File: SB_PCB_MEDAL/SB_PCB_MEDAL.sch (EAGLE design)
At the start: 41 parts, among them IC1 ATTINY44A-SSU

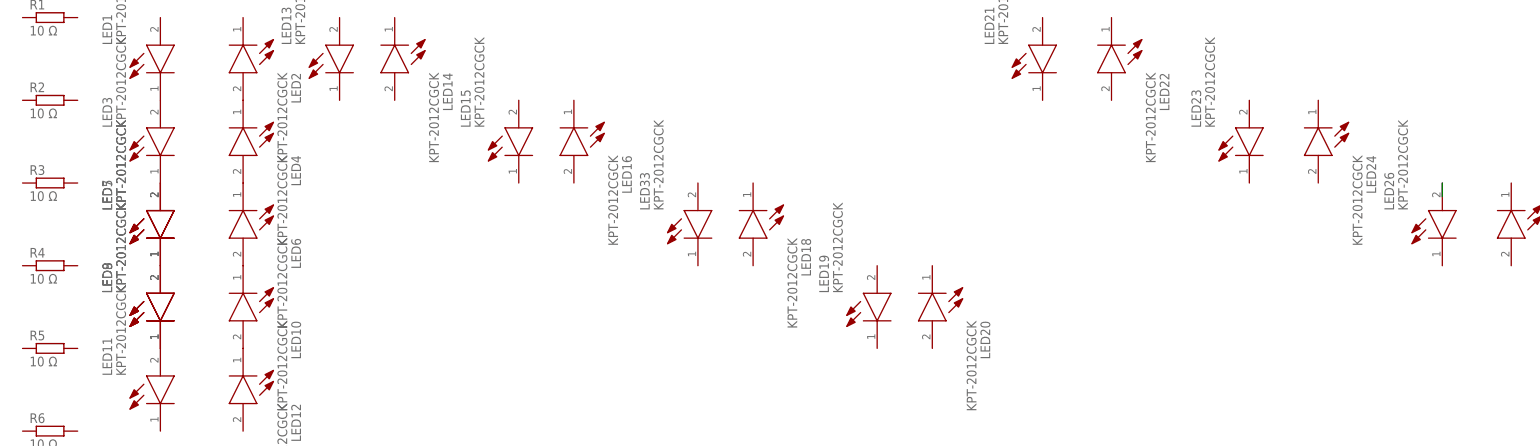
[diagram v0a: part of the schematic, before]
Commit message: removed 2 additional LEDs
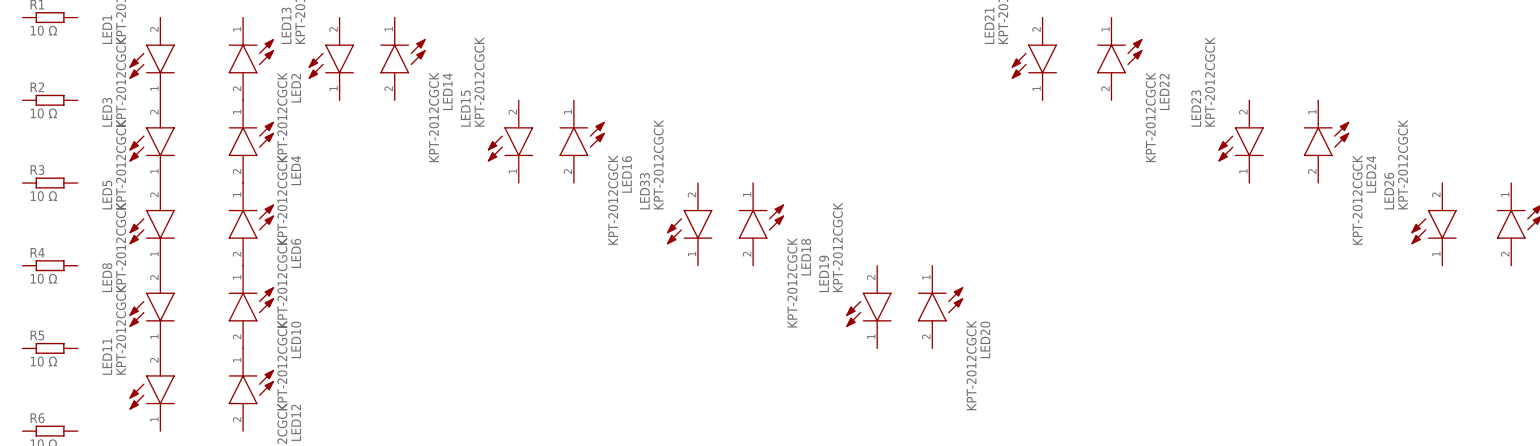
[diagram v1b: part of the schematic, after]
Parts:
- removed LED7, LED9: KPT-2012CGCK, SamacSys_Parts:KPT-2012CGCK
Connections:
- removed net N$1: LED26.A
- net N$2: no longer LED7.A
- net N$4: no longer LED7.K, LED9.A
- net N$5: no longer LED9.K
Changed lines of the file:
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@@
 <?xml version="1.0" encoding="utf-8"?>
 <!DOCTYPE eagle SYSTEM "eagle.dtd">
-<eagle version="7.6.0">
+<eagle version="8.4.1">
 <drawing>
 <settings>
 <setting alwaysvectorfont="no"/>
+<setting keepoldvectorfont="yes"/>
 <setting verticaltext="up"/>
 </settings>
@@
 <part name="LED5" library="SamacSys_Parts" deviceset="KPT-2012CGCK" device=""/>
 <part name="LED6" library="SamacSys_Parts" deviceset="KPT-2012CGCK" device=""/>
-<part name="LED7" library="SamacSys_Parts" deviceset="KPT-2012CGCK" device=""/>
 <part name="LED8" library="SamacSys_Parts" deviceset="KPT-2012CGCK" device=""/>
-<part name="LED9" library="SamacSys_Parts" deviceset="KPT-2012CGCK" device=""/>
 <part name="LED10" library="SamacSys_Parts" deviceset="KPT-2012CGCK" device=""/>
 <part name="LED11" library="SamacSys_Parts" deviceset="KPT-2012CGCK" device=""/>
@@
 <instance part="LED5" gate="G$1" x="144.78" y="25.4" rot="R90"/>
 <instance part="LED6" gate="G$1" x="160.02" y="40.64" rot="R270"/>
-<instance part="LED7" gate="G$1" x="144.78" y="25.4" rot="R90"/>
 <instance part="LED8" gate="G$1" x="144.78" y="10.16" rot="R90"/>
-<instance part="LED9" gate="G$1" x="144.78" y="10.16" rot="R90"/>
 <instance part="LED10" gate="G$1" x="160.02" y="25.4" rot="R270"/>
 <instance part="LED11" gate="G$1" x="144.78" y="-5.08" rot="R90"/>
@@
 </segment>
 </net>
-<net name="N$1" class="0">
-<segment>
-<pinref part="LED26" gate="G$1" pin="A"/>
-<wire x1="381" y1="40.64" x2="381" y2="38.1" width="0.1524" layer="91"/>
-</segment>
-</net>
 <net name="N$3" class="0">
 <segment>
@@
 <pinref part="LED3" gate="G$1" pin="K"/>
 <pinref part="LED5" gate="G$1" pin="A"/>
-<pinref part="LED7" gate="G$1" pin="A"/>
 </segment>
 </net>
@@
 <segment>
 <pinref part="LED5" gate="G$1" pin="K"/>
-<pinref part="LED7" gate="G$1" pin="K"/>
 <pinref part="LED8" gate="G$1" pin="A"/>
-<pinref part="LED9" gate="G$1" pin="A"/>
 </segment>
 </net>
@@
 <segment>
 <pinref part="LED8" gate="G$1" pin="K"/>
-<pinref part="LED9" gate="G$1" pin="K"/>
 <pinref part="LED11" gate="G$1" pin="A"/>
 </segment>

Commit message: literally copy and paste files from other branch into the master because EAGLE files and branches hate each other as much as North Korea and the US....
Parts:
- removed LED31, LED32, LED33: KPT-2012CGCK, SamacSys_Parts:KPT-2012CGCK
- added LED17, LED7, LED9: KPT-2012CGCK, SamacSys_Parts:KPT-2012CGCK
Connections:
- removed net N$10: LED2.A, LED4.K
- removed net N$7: LED10.K, LED6.A
- removed net N$8: LED4.A, LED6.K
- new net N$1: LED1.A, LED11.A, LED12.K, LED19.A, LED2.K, LED20.K, LED25.A, LED26.K, LED29.A, LED30.K, R1.2
- new net N$19: IC1.[PCINT10/INT0/OC0A/CKOUT]PB2
- new net N$20: IC1.[PCINT7/ICP/OC0B/ADC7]PA7
- new net PA0: IC1.PA0[ADC0/AREF/PCINT0], R1.1
- new net PA1: IC1.PA1[ADC1/AIN0/PCINT1], R2.1
- new net PA2: IC1.PA2[ADC2/AIN1/PCINT2], R3.1
- new net PA3: IC1.PA3[ADC3/T0/PCINT3], R4.1
- new net PB0: IC1.[PCINT8/XTAL1/CLKI]PB0, R5.1
- new net PB1: IC1.[PCINT9/XTAL2]PB1, R6.1
- net N$2: now also LED1.K, LED13.A, LED14.K, LED2.A, LED21.A, LED22.K, LED27.A, LED28.K, LED3.A, LED4.K, R2.2; no longer LED3.K, LED5.A
- net N$3: now also LED11.K, LED12.A, LED15.A, LED16.K, LED23.A, LED24.K, LED3.K, LED4.A, LED5.A, LED6.K, R3.2; no longer LED1.K, LED3.A
- net N$4: now also LED13.K, LED14.A, LED17.A, LED18.K, LED19.K, LED20.A, LED6.A, LED7.A, LED8.K, R4.2; no longer LED8.A
- net N$5: now also LED10.K, LED15.K, LED16.A, LED21.K, LED22.A, LED25.K, LED26.A, LED7.K, LED8.A, LED9.A, R5.2; no longer LED11.A, LED8.K
- net N$6: now also LED17.K, LED18.A, LED23.K, LED24.A, LED27.K, LED28.A, LED29.K, LED30.A, LED9.K, R6.2; no longer LED12.K
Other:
- note added: "PA0"
- note added: "PA1"
- note added: "PA2"
- note added: "PA3"
- note added: "PB0"
- note added: "PB1"
- moved on the sheet: LED1, LED10, LED11, LED12, LED13, LED14, LED15, LED16, LED18, LED19, LED2, LED20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

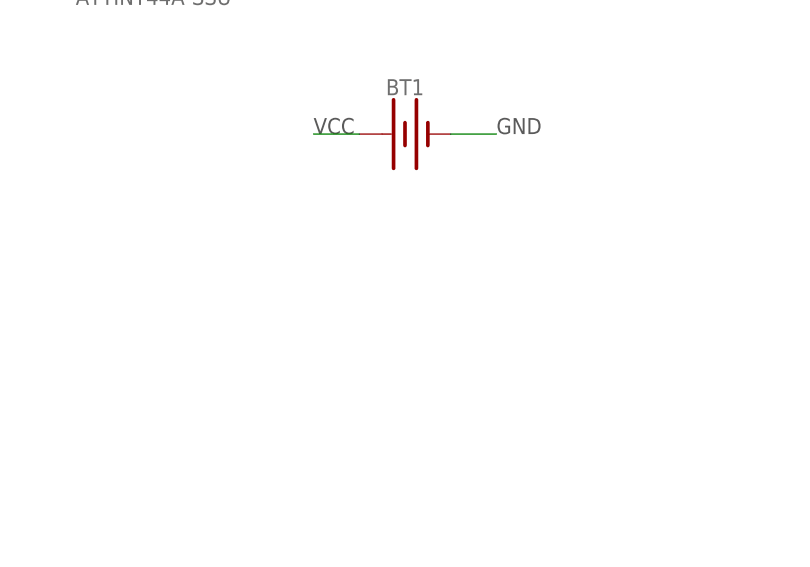
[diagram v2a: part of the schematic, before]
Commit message: added surface mountable button
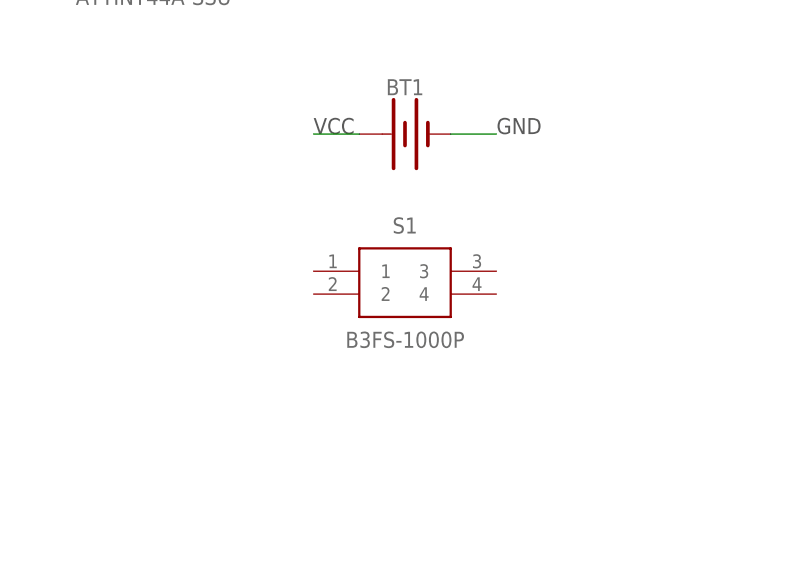
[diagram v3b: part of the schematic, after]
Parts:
- added S1: B3FS-1000P, SamacSys_Parts:B3FS-1000P
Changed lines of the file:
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@@
 <part name="LED29" library="SamacSys_Parts" deviceset="KPT-2012CGCK" device=""/>
 <part name="LED30" library="SamacSys_Parts" deviceset="KPT-2012CGCK" device=""/>
+<part name="S1" library="SamacSys_Parts" deviceset="B3FS-1000P" device=""/>
 </parts>
 <sheets>
@@
 <instance part="LED29" gate="G$1" x="431.8" y="66.04" rot="R90"/>
 <instance part="LED30" gate="G$1" x="441.96" y="81.28" rot="R270"/>
+<instance part="S1" gate="G$1" x="58.42" y="15.24"/>
 </instances>
 <busses>

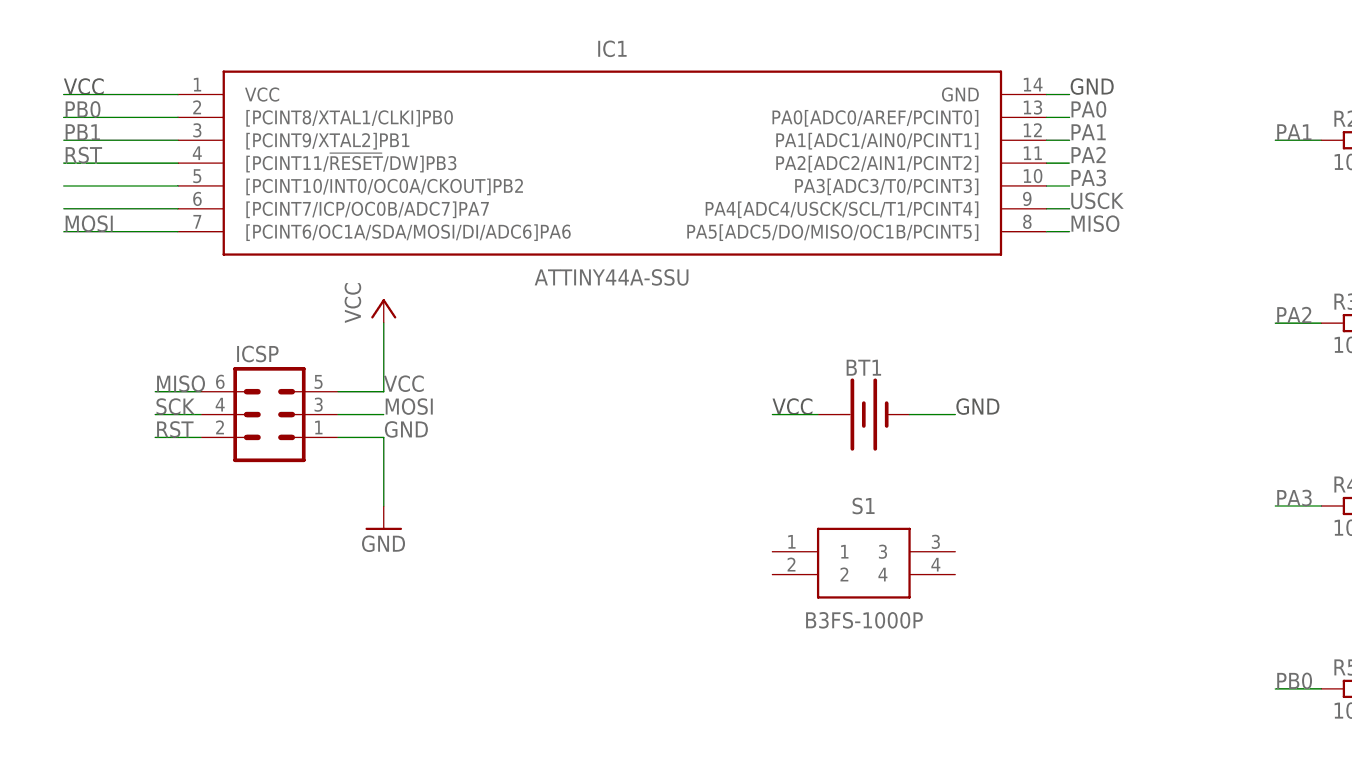
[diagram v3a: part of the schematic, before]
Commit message: added more labels to the board
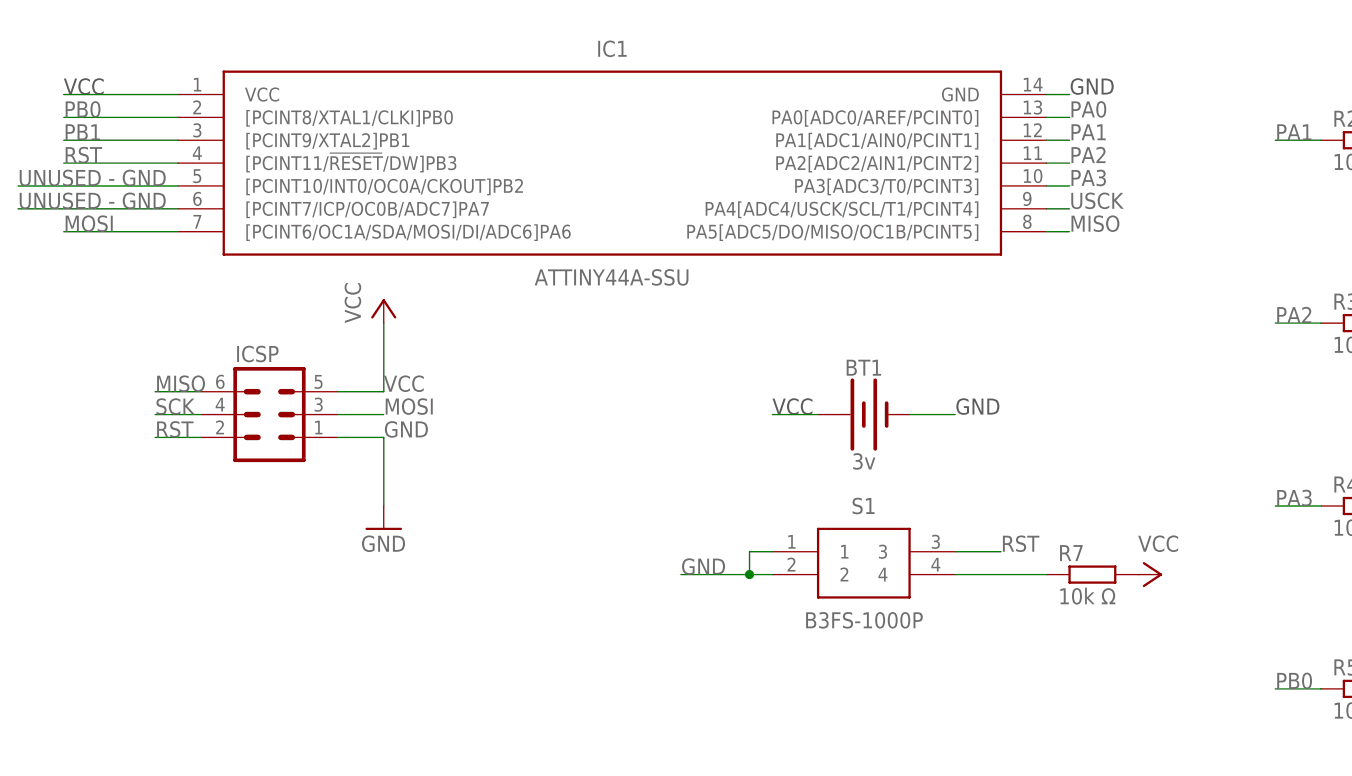
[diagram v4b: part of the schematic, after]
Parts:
- added R7: 10k Ω, resistor:R-EU_M0805
- BT1: value (none) -> 3v
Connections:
- removed net N$19: IC1.[PCINT10/INT0/OC0A/CKOUT]PB2
- removed net N$20: IC1.[PCINT7/ICP/OC0B/ADC7]PA7
- new net N$7: R7.1, S1.4
- new net N$8: S1.3
- net GND: now also IC1.[PCINT10/INT0/OC0A/CKOUT]PB2, IC1.[PCINT7/ICP/OC0B/ADC7]PA7, S1.1, S1.2
- net VCC: now also R7.2
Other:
- note added: "UNUSED - GND"
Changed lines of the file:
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@@
 <part name="GND1" library="supply1" deviceset="GND" device=""/>
 <part name="P+1" library="supply1" deviceset="VCC" device=""/>
-<part name="BT1" library="SparkFun-Batteries" deviceset="BATTERY" device="-12MM_PTH"/>
+<part name="BT1" library="SparkFun-Batteries" deviceset="BATTERY" device="-12MM_PTH" value="3v"/>
 <part name="LED1" library="SamacSys_Parts" deviceset="KPT-2012CGCK" device=""/>
 <part name="LED2" library="SamacSys_Parts" deviceset="KPT-2012CGCK" device=""/>
@@
 <part name="LED30" library="SamacSys_Parts" deviceset="KPT-2012CGCK" device=""/>
 <part name="S1" library="SamacSys_Parts" deviceset="B3FS-1000P" device=""/>
+<part name="R7" library="resistor" deviceset="R-EU_" device="M0805" value="10k Ω"/>
+<part name="P+2" library="supply1" library_urn="urn:adsk.eagle:library:371" deviceset="VCC" device=""/>
 </parts>
 <sheets>
@@
 <text x="114.3" y="0" size="1.778" layer="95">PB0</text>
 <text x="114.3" y="-20.32" size="1.778" layer="95">PB1</text>
+<text x="-25.4" y="55.88" size="1.778" layer="95">UNUSED - GND</text>
+<text x="-25.4" y="53.34" size="1.778" layer="95">UNUSED - GND</text>
+<text x="83.82" y="15.24" size="1.778" layer="95">RST</text>
+<text x="48.26" y="12.7" size="1.778" layer="95">GND</text>
 </plain>
 <instances>
@@
 <instance part="LED30" gate="G$1" x="441.96" y="81.28" rot="R270"/>
 <instance part="S1" gate="G$1" x="58.42" y="15.24"/>
+<instance part="R7" gate="G$1" x="93.98" y="12.7"/>
+<instance part="P+2" gate="VCC" x="101.6" y="12.7" rot="R270"/>
 </instances>
 <busses>
@@
 <wire x1="73.66" y1="30.48" x2="78.74" y2="30.48" width="0.1524" layer="91"/>
 </segment>
+<segment>
+<pinref part="IC1" gate="G$1" pin="[PCINT10/INT0/OC0A/CKOUT]PB2"/>
+<wire x1="-7.62" y1="55.88" x2="-25.4" y2="55.88" width="0.1524" layer="91"/>
+</segment>
+<segment>
+<pinref part="IC1" gate="G$1" pin="[PCINT7/ICP/OC0B/ADC7]PA7"/>
+<wire x1="-7.62" y1="53.34" x2="-25.4" y2="53.34" width="0.1524" layer="91"/>
+</segment>
+<segment>
+<pinref part="S1" gate="G$1" pin="2"/>
+<wire x1="58.42" y1="12.7" x2="55.88" y2="12.7" width="0.1524" layer="91"/>
+<pinref part="S1" gate="G$1" pin="1"/>
+<wire x1="55.88" y1="12.7" x2="48.26" y2="12.7" width="0.1524" layer="91"/>
+<wire x1="58.42" y1="15.24" x2="55.88" y2="15.24" width="0.1524" layer="91"/>
+<wire x1="55.88" y1="15.24" x2="55.88" y2="12.7" width="0.1524" layer="91"/>
+<junction x="55.88" y="12.7"/>
+</segment>
 </net>
 <net name="VCC" class="0">
@@
 <pinref part="BT1" gate="G$1" pin="+"/>
 <wire x1="63.5" y1="30.48" x2="58.42" y2="30.48" width="0.1524" layer="91"/>
+</segment>
+<segment>
+<pinref part="R7" gate="G$1" pin="2"/>
+<pinref part="P+2" gate="VCC" pin="VCC"/>
 </segment>
 </net>
@@
 </segment>
 </net>
-<net name="N$19" class="0">
-<segment>
-<pinref part="IC1" gate="G$1" pin="[PCINT10/INT0/OC0A/CKOUT]PB2"/>
-<wire x1="-7.62" y1="55.88" x2="-20.32" y2="55.88" width="0.1524" layer="91"/>
-</segment>
-</net>
-<net name="N$20" class="0">
-<segment>
-<pinref part="IC1" gate="G$1" pin="[PCINT7/ICP/OC0B/ADC7]PA7"/>
-<wire x1="-7.62" y1="53.34" x2="-20.32" y2="53.34" width="0.1524" layer="91"/>
+<net name="N$7" class="0">
+<segment>
+<pinref part="S1" gate="G$1" pin="4"/>
+<pinref part="R7" gate="G$1" pin="1"/>
+<wire x1="78.74" y1="12.7" x2="88.9" y2="12.7" width="0.1524" layer="91"/>
+</segment>
+</net>
+<net name="N$8" class="0">
+<segment>
+<pinref part="S1" gate="G$1" pin="3"/>
+<wire x1="78.74" y1="15.24" x2="83.82" y2="15.24" width="0.1524" layer="91"/>
 </segment>
 </net>
@@
 </sheet>
 </sheets>
+<errors>
+</errors>
 </schematic>
 </drawing>
@@
 which will not be processed correctly with this version.
 </note>
+<note version="8.2" severity="warning">
+Since Version 8.2, EAGLE supports online libraries. The ids
+of those online libraries will not be understood (or retained)
+with this version.
+</note>
+<note version="8.3" severity="warning">
+Since Version 8.3, EAGLE supports URNs for individual library
+assets (packages, symbols, and devices). The URNs of those assets
+will not be understood (or retained) with this version.
+</note>
 </compatibility>

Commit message: modify led position and add usb
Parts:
- removed BT1: 3v, SparkFun-Batteries:BATTERY-12MM_PTH
- removed IC1: ATTINY44A-SSU, SamacSys_Parts:ATTINY44A-SSU
- removed R7: 10k Ω, resistor:R-EU_M0805
- removed S1: B3FS-1000P, SamacSys_Parts:B3FS-1000P
- added U1: ATMEGA16U2-AU, Atmel_By_element14_Batch_1-00:ATMEGA16U2-AU
- added X1: MINI-USB_SHIELD5P2-32005-601, con-cypressindustries:MINI-USB_SHIELD5P2-32005-601
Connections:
- removed net N$7: R7.1, S1.4
- removed net N$8: S1.3
- net GND: no longer BT1.-, IC1.GND, IC1.[PCINT10/INT0/OC0A/CKOUT]PB2, IC1.[PCINT7/ICP/OC0B/ADC7]PA7, S1.1, S1.2
- net MISO: no longer IC1.PA5[ADC5/DO/MISO/OC1B/PCINT5]
- net MOSI: no longer IC1.[PCINT6/OC1A/SDA/MOSI/DI/ADC6]PA6
- net PA0: no longer IC1.PA0[ADC0/AREF/PCINT0]
- net PA1: no longer IC1.PA1[ADC1/AIN0/PCINT1]
- net PA2: no longer IC1.PA2[ADC2/AIN1/PCINT2]
- net PA3: no longer IC1.PA3[ADC3/T0/PCINT3]
- net PB0: no longer IC1.[PCINT8/XTAL1/CLKI]PB0
- net PB1: no longer IC1.[PCINT9/XTAL2]PB1
- net RST: no longer IC1.[PCINT11/!RESET!/DW]PB3
- net USCK: no longer IC1.PA4[ADC4/USCK/SCL/T1/PCINT4]
- net VCC: no longer BT1.+, IC1.VCC, R7.2
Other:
- note added: "1"
- note added: "ATMEGA16U2-AU Microcontroller"
- note added: "Anton Nikitin - Henry Oliver-Edwards"
- note added: "Battery"
- note added: "CC 2.5 BY/SA"
- note added: "Charlieplexing Circuit for LEDs"
- note added: "ICSP Header"
- note added: "SourceBots - PCB Medals"
- note added: "USB"
- note added: "v1.0"
- note removed: "SourceBots - PCB Medal Schematic Version 1.0 Anton Nikitin - Henry Oliver-Edwards"
- note removed: "UNUSED - GND"
- note removed: "USCK"
- moved on the sheet: ICSP, LED1, LED10, LED11, LED12, LED13, LED14, LED15, LED16, LED17, LED18, LED19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

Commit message: modify boards
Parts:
- added Y1: FOXSDLF_120-20, SamacSys_Parts:FOXSDLF_120-20
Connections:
- new net N$7: Y1.1
- new net N$8: Y1.2
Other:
- note added: "12MHz Crystal Oscillator"
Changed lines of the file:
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@@
 <part name="U1" library="Atmel_By_element14_Batch_1-00" deviceset="ATMEGA16U2-AU" device=""/>
 <part name="FRAME1" library="frames" deviceset="DOCFIELD" device=""/>
-<part name="X1" library="con-cypressindustries" library_urn="urn:adsk.eagle:library:138" deviceset="MINI-USB_SHIELD5P2-" device="32005-601" package3d_urn="urn:adsk.eagle:package:6465/1"/>
+<part name="X1" library="con-cypressindustries" library_urn="urn:adsk.eagle:library:138" deviceset="MINI-USB_SHIELD5P2-" device="32005-601" package3d_urn="urn:adsk.eagle:package:6465/1" value=""/>
+<part name="Y1" library="SamacSys_Parts" deviceset="FOXSDLF_120-20" device=""/>
 </parts>
 <sheets>
@@
 <wire x1="53.34" y1="-76.2" x2="53.34" y2="-27.94" width="0.1524" layer="95" style="shortdash"/>
 <text x="53.34" y="-25.4" size="1.778" layer="95">USB</text>
+<wire x1="-111.76" y1="-33.02" x2="-58.42" y2="-33.02" width="0.1524" layer="95" style="shortdash"/>
+<wire x1="-58.42" y1="-33.02" x2="-58.42" y2="-55.88" width="0.1524" layer="95" style="shortdash"/>
+<wire x1="-58.42" y1="-55.88" x2="-111.76" y2="-55.88" width="0.1524" layer="95" style="shortdash"/>
+<wire x1="-111.76" y1="-55.88" x2="-111.76" y2="-33.02" width="0.1524" layer="95" style="shortdash"/>
+<text x="-101.6" y="-30.48" size="1.778" layer="95">12MHz Crystal Oscillator</text>
 </plain>
 <instances>
@@
 <instance part="FRAME1" gate="G$1" x="106.68" y="-86.36"/>
 <instance part="X1" gate="G41" x="73.66" y="-60.96"/>
+<instance part="Y1" gate="G$1" x="-96.52" y="-45.72"/>
 </instances>
 <busses>
@@
 </segment>
 </net>
+<net name="N$7" class="0">
+<segment>
+<pinref part="Y1" gate="G$1" pin="1"/>
+<wire x1="-96.52" y1="-45.72" x2="-104.14" y2="-45.72" width="0.1524" layer="91"/>
+<label x="-104.14" y="-45.72" size="1.778" layer="95"/>
+</segment>
+</net>
+<net name="N$8" class="0">
+<segment>
+<pinref part="Y1" gate="G$1" pin="2"/>
+<wire x1="-76.2" y1="-45.72" x2="-68.58" y2="-45.72" width="0.1524" layer="91"/>
+<label x="-68.58" y="-45.72" size="1.778" layer="95"/>
+</segment>
+</net>
